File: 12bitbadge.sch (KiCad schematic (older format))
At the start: 44 parts, among them J1 Conn_02x04_Counter_Clockwise, J2 Conn_02x04_Counter_Clockwise, J3 Conn_02x04_Counter_Clockwise, J4 Conn_02x03_Odd_Even, J5 Conn_02x03_Odd_Even, J6 Conn_02x03_Odd_Even, J7 Conn_02x03_Odd_Even, SW1 SW_SPDT, SW10 SW_SPDT, SW11 SW_SPDT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

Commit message: Updated to hand-solderable SMD
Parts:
- R1, R10, R11, R12, R13, R14, R15, R16, R17, R18, R2, R3, R4, R5, R6, R7, R8, R9: footprint Resistor_SMD:R_0805_2012Metric -> Resistor_SMD:R_0805_2012Metric_Pad1.15x1.40mm_HandSolder
- U1, U2, U3: footprint Package_TO_SOT_SMD:SOT-23-6 -> Package_TO_SOT_SMD:SOT-23-6_Handsoldering
- U4, U5, U6: footprint Package_TO_SOT_SMD:SOT-23-5 -> Package_TO_SOT_SMD:SOT-23-5_HandSoldering
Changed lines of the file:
@@
 F 0 "U1" H 2700 1325 50  0000 R CNN
 F 1 "ATtiny10-TS" H 2700 1250 50  0000 R CNN
-F 2 "Package_TO_SOT_SMD:SOT-23-6" H 2725 1300 50  0001 C CIN
+F 2 "Package_TO_SOT_SMD:SOT-23-6_Handsoldering" H 2725 1300 50  0001 C CIN
 F 3 "http://ww1.microchip.com/downloads/en/DeviceDoc/Atmel-8127-AVR-8-bit-Microcontroller-ATtiny4-ATtiny5-ATtiny9-ATtiny10_Datasheet.pdf" H 2725 1300 50  0001 C CNN
 	1    2725 1300
@@
 F 0 "U2" H 2400 3100 50  0000 R CNN
 F 1 "ATtiny10-TS" H 2700 3000 50  0000 R CNN
-F 2 "Package_TO_SOT_SMD:SOT-23-6" H 2725 3050 50  0001 C CIN
+F 2 "Package_TO_SOT_SMD:SOT-23-6_Handsoldering" H 2725 3050 50  0001 C CIN
 F 3 "http://ww1.microchip.com/downloads/en/DeviceDoc/Atmel-8127-AVR-8-bit-Microcontroller-ATtiny4-ATtiny5-ATtiny9-ATtiny10_Datasheet.pdf" H 2725 3050 50  0001 C CNN
 	1    2725 3050
@@
 F 0 "U3" H 2375 5175 50  0000 R CNN
 F 1 "ATtiny10-TS" H 2550 5075 50  0000 R CNN
-F 2 "Package_TO_SOT_SMD:SOT-23-6" H 2575 5125 50  0001 C CIN
+F 2 "Package_TO_SOT_SMD:SOT-23-6_Handsoldering" H 2575 5125 50  0001 C CIN
 F 3 "http://ww1.microchip.com/downloads/en/DeviceDoc/Atmel-8127-AVR-8-bit-Microcontroller-ATtiny4-ATtiny5-ATtiny9-ATtiny10_Datasheet.pdf" H 2575 5125 50  0001 C CNN
 	1    2575 5125
@@
 F 0 "R2" V 5943 950 50  0000 C CNN
 F 1 "50k" V 6034 950 50  0000 C CNN
-F 2 "Resistor_SMD:R_0805_2012Metric" V 6080 950 50  0001 C CNN
+F 2 "Resistor_SMD:R_0805_2012Metric_Pad1.15x1.40mm_HandSolder" V 6080 950 50  0001 C CNN
 F 3 "~" H 6150 950 50  0001 C CNN
 	1    6150 950
@@
 F 0 "R3" V 6768 950 50  0000 C CNN
 F 1 "100k" V 6859 950 50  0000 C CNN
-F 2 "Resistor_SMD:R_0805_2012Metric" V 6905 950 50  0001 C CNN
+F 2 "Resistor_SMD:R_0805_2012Metric_Pad1.15x1.40mm_HandSolder" V 6905 950 50  0001 C CNN
 F 3 "~" H 6975 950 50  0001 C CNN
 	1    6975 950
@@
 F 0 "R4" V 7593 950 50  0000 C CNN
 F 1 "200k" V 7684 950 50  0000 C CNN
-F 2 "Resistor_SMD:R_0805_2012Metric" V 7730 950 50  0001 C CNN
+F 2 "Resistor_SMD:R_0805_2012Metric_Pad1.15x1.40mm_HandSolder" V 7730 950 50  0001 C CNN
 F 3 "~" H 7800 950 50  0001 C CNN
 	1    7800 950
@@
 F 0 "R1" V 5118 950 50  0000 C CNN
 F 1 "25k" V 5209 950 50  0000 C CNN
-F 2 "Resistor_SMD:R_0805_2012Metric" V 5255 950 50  0001 C CNN
+F 2 "Resistor_SMD:R_0805_2012Metric_Pad1.15x1.40mm_HandSolder" V 5255 950 50  0001 C CNN
 F 3 "~" H 5325 950 50  0001 C CNN
 	1    5325 950
@@
 F 0 "R5" H 8430 1254 50  0000 R CNN
 F 1 "25k" H 8430 1345 50  0000 R CNN
-F 2 "Resistor_SMD:R_0805_2012Metric" V 8430 1300 50  0001 C CNN
+F 2 "Resistor_SMD:R_0805_2012Metric_Pad1.15x1.40mm_HandSolder" V 8430 1300 50  0001 C CNN
 F 3 "~" H 8500 1300 50  0001 C CNN
 	1    8500 1300
@@
 F 0 "R7" V 5943 2850 50  0000 C CNN
 F 1 "50k" V 6034 2850 50  0000 C CNN
-F 2 "Resistor_SMD:R_0805_2012Metric" V 6080 2850 50  0001 C CNN
+F 2 "Resistor_SMD:R_0805_2012Metric_Pad1.15x1.40mm_HandSolder" V 6080 2850 50  0001 C CNN
 F 3 "~" H 6150 2850 50  0001 C CNN
 	1    6150 2850
@@
 F 0 "R8" V 6768 2850 50  0000 C CNN
 F 1 "100k" V 6859 2850 50  0000 C CNN
-F 2 "Resistor_SMD:R_0805_2012Metric" V 6905 2850 50  0001 C CNN
+F 2 "Resistor_SMD:R_0805_2012Metric_Pad1.15x1.40mm_HandSolder" V 6905 2850 50  0001 C CNN
 F 3 "~" H 6975 2850 50  0001 C CNN
 	1    6975 2850
@@
 F 0 "R9" V 7593 2850 50  0000 C CNN
 F 1 "200k" V 7684 2850 50  0000 C CNN
-F 2 "Resistor_SMD:R_0805_2012Metric" V 7730 2850 50  0001 C CNN
+F 2 "Resistor_SMD:R_0805_2012Metric_Pad1.15x1.40mm_HandSolder" V 7730 2850 50  0001 C CNN
 F 3 "~" H 7800 2850 50  0001 C CNN
 	1    7800 2850
@@
 F 0 "R6" V 5118 2850 50  0000 C CNN
 F 1 "25k" V 5209 2850 50  0000 C CNN
-F 2 "Resistor_SMD:R_0805_2012Metric" V 5255 2850 50  0001 C CNN
+F 2 "Resistor_SMD:R_0805_2012Metric_Pad1.15x1.40mm_HandSolder" V 5255 2850 50  0001 C CNN
 F 3 "~" H 5325 2850 50  0001 C CNN
 	1    5325 2850
@@
 F 0 "R10" H 8430 3154 50  0000 R CNN
 F 1 "25k" H 8430 3245 50  0000 R CNN
-F 2 "Resistor_SMD:R_0805_2012Metric" V 8430 3200 50  0001 C CNN
+F 2 "Resistor_SMD:R_0805_2012Metric_Pad1.15x1.40mm_HandSolder" V 8430 3200 50  0001 C CNN
 F 3 "~" H 8500 3200 50  0001 C CNN
 	1    8500 3200
@@
 F 0 "R12" V 5768 5025 50  0000 C CNN
 F 1 "50k" V 5859 5025 50  0000 C CNN
-F 2 "Resistor_SMD:R_0805_2012Metric" V 5905 5025 50  0001 C CNN
+F 2 "Resistor_SMD:R_0805_2012Metric_Pad1.15x1.40mm_HandSolder" V 5905 5025 50  0001 C CNN
 F 3 "~" H 5975 5025 50  0001 C CNN
 	1    5975 5025
@@
 F 0 "R13" V 6593 5025 50  0000 C CNN
 F 1 "100k" V 6684 5025 50  0000 C CNN
-F 2 "Resistor_SMD:R_0805_2012Metric" V 6730 5025 50  0001 C CNN
+F 2 "Resistor_SMD:R_0805_2012Metric_Pad1.15x1.40mm_HandSolder" V 6730 5025 50  0001 C CNN
 F 3 "~" H 6800 5025 50  0001 C CNN
 	1    6800 5025
@@
 F 0 "R14" V 7418 5025 50  0000 C CNN
 F 1 "200k" V 7509 5025 50  0000 C CNN
-F 2 "Resistor_SMD:R_0805_2012Metric" V 7555 5025 50  0001 C CNN
+F 2 "Resistor_SMD:R_0805_2012Metric_Pad1.15x1.40mm_HandSolder" V 7555 5025 50  0001 C CNN
 F 3 "~" H 7625 5025 50  0001 C CNN
 	1    7625 5025
@@
 F 0 "R11" V 4943 5025 50  0000 C CNN
 F 1 "25k" V 5034 5025 50  0000 C CNN
-F 2 "Resistor_SMD:R_0805_2012Metric" V 5080 5025 50  0001 C CNN
+F 2 "Resistor_SMD:R_0805_2012Metric_Pad1.15x1.40mm_HandSolder" V 5080 5025 50  0001 C CNN
 F 3 "~" H 5150 5025 50  0001 C CNN
 	1    5150 5025
@@
 F 0 "R15" H 8255 5329 50  0000 R CNN
 F 1 "25k" H 8255 5420 50  0000 R CNN
-F 2 "Resistor_SMD:R_0805_2012Metric" V 8255 5375 50  0001 C CNN
+F 2 "Resistor_SMD:R_0805_2012Metric_Pad1.15x1.40mm_HandSolder" V 8255 5375 50  0001 C CNN
 F 3 "~" H 8325 5375 50  0001 C CNN
 	1    8325 5375
@@
 F 0 "R16" V 3550 7125 50  0000 C CNN
 F 1 "1k" V 3625 7125 50  0000 C CNN
-F 2 "Resistor_SMD:R_0805_2012Metric" V 3555 7125 50  0001 C CNN
+F 2 "Resistor_SMD:R_0805_2012Metric_Pad1.15x1.40mm_HandSolder" V 3555 7125 50  0001 C CNN
 F 3 "~" H 3625 7125 50  0001 C CNN
 	1    3625 7125
@@
 F 0 "R17" V 3550 7325 50  0000 C CNN
 F 1 "1k" V 3625 7325 50  0000 C CNN
-F 2 "Resistor_SMD:R_0805_2012Metric" V 3555 7325 50  0001 C CNN
+F 2 "Resistor_SMD:R_0805_2012Metric_Pad1.15x1.40mm_HandSolder" V 3555 7325 50  0001 C CNN
 F 3 "~" H 3625 7325 50  0001 C CNN
 	1    3625 7325
@@
 F 0 "R18" V 3550 7525 50  0000 C CNN
 F 1 "1k" V 3625 7525 50  0000 C CNN
-F 2 "Resistor_SMD:R_0805_2012Metric" V 3555 7525 50  0001 C CNN
+F 2 "Resistor_SMD:R_0805_2012Metric_Pad1.15x1.40mm_HandSolder" V 3555 7525 50  0001 C CNN
 F 3 "~" H 3625 7525 50  0001 C CNN
 	1    3625 7525
@@
 F 0 "U4" H 10025 1817 50  0000 C CNN
 F 1 "TPS2041B" H 10025 1726 50  0000 C CNN
-F 2 "Package_TO_SOT_SMD:SOT-23-5" H 10025 1850 50  0001 C CNN
+F 2 "Package_TO_SOT_SMD:SOT-23-5_HandSoldering" H 10025 1850 50  0001 C CNN
 F 3 "http://www.ti.com/lit/ds/symlink/tps2041.pdf" H 9975 1650 50  0001 C CNN
 	1    10025 1350
@@
 F 0 "U5" H 10075 3792 50  0000 C CNN
 F 1 "TPS2041B" H 10075 3701 50  0000 C CNN
-F 2 "Package_TO_SOT_SMD:SOT-23-5" H 10075 3825 50  0001 C CNN
+F 2 "Package_TO_SOT_SMD:SOT-23-5_HandSoldering" H 10075 3825 50  0001 C CNN
 F 3 "http://www.ti.com/lit/ds/symlink/tps2041.pdf" H 10025 3625 50  0001 C CNN
 	1    10075 3325
@@
 F 0 "U6" H 10000 5992 50  0000 C CNN
 F 1 "TPS2041B" H 10000 5901 50  0000 C CNN
-F 2 "Package_TO_SOT_SMD:SOT-23-5" H 10000 6025 50  0001 C CNN
+F 2 "Package_TO_SOT_SMD:SOT-23-5_HandSoldering" H 10000 6025 50  0001 C CNN
 F 3 "http://www.ti.com/lit/ds/symlink/tps2041.pdf" H 9950 5825 50  0001 C CNN
 	1    10000 5525

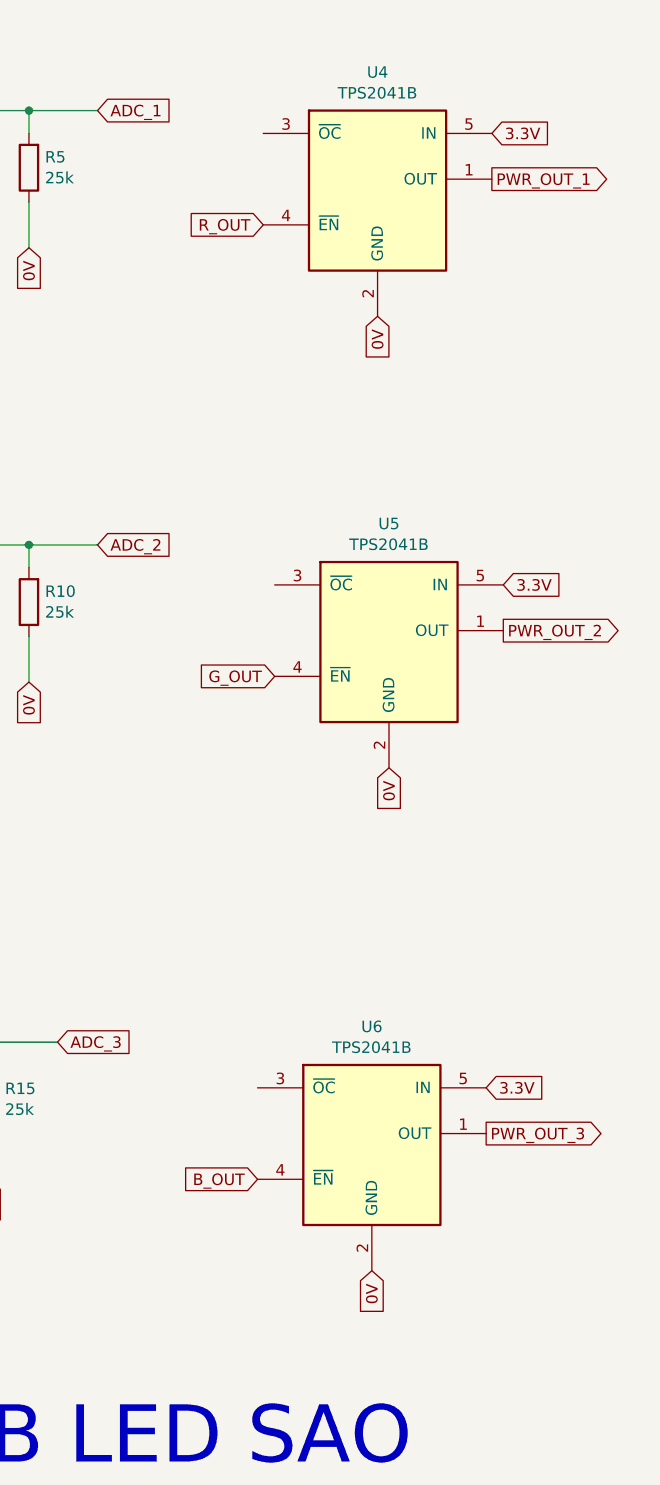
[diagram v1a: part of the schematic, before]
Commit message: Replaced switches with PWM-friendly MOSFETs
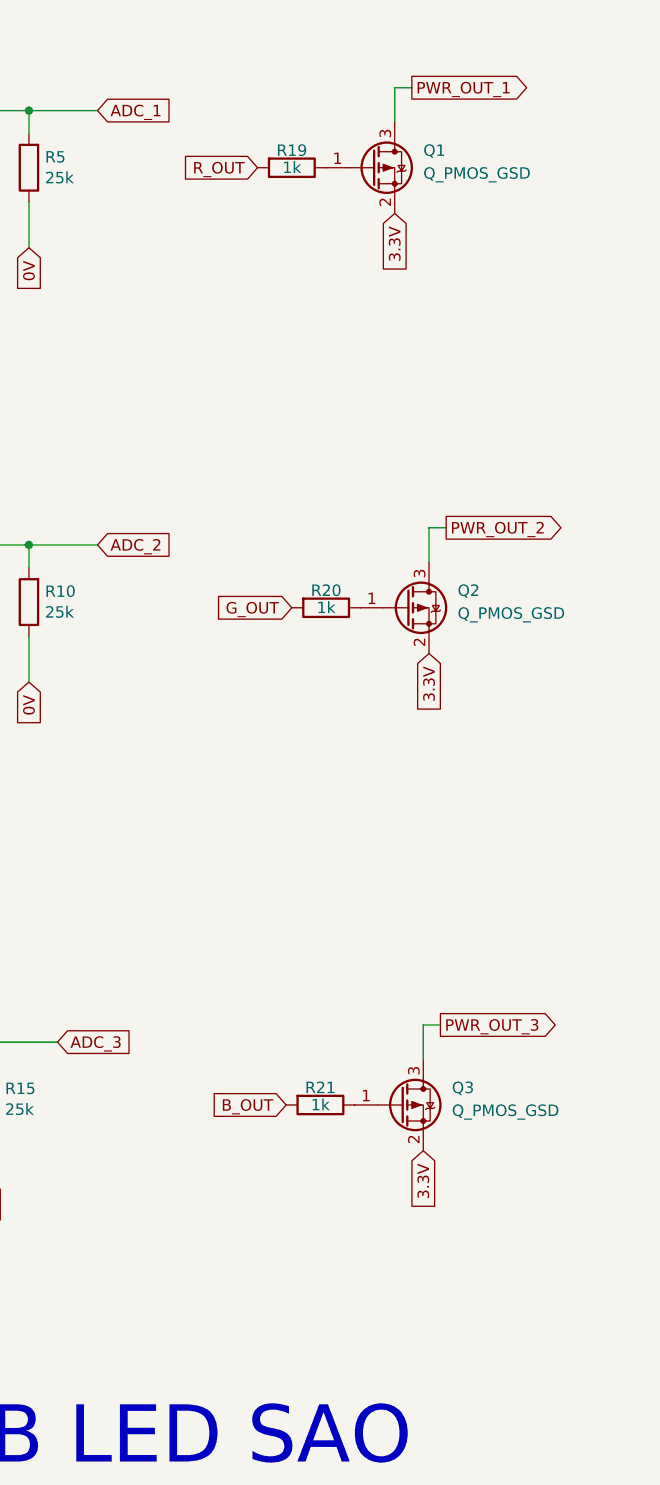
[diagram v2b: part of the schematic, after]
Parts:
- removed U4, U5, U6: TPS2041B, Package_TO_SOT_SMD:SOT-23-5_HandSoldering, symbol Power_Management:TPS2041B
- added Q1, Q2, Q3: Q_PMOS_GSD, Package_TO_SOT_SMD:SOT-23, symbol Device:Q_PMOS_GSD
- added R19, R20, R21: 1k, Resistor_SMD:R_0805_2012Metric_Pad1.15x1.40mm_HandSolder, symbol Device:R
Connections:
- net 3.3V: now also Q1.2 (S), Q2.2 (S), Q3.2 (S)
- net B_OUT: now also R21.2
- net G_OUT: now also R20.2
- net PWR_OUT_1: now also Q1.3 (D)
- net PWR_OUT_2: now also Q2.3 (D)
- net PWR_OUT_3: now also Q3.3 (D)
- net R_OUT: now also R19.2
- new net: Q2.1 (G), R20.1
- new net: Q1.1 (G), R19.1
- new net: Q3.1 (G), R21.1
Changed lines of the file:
@@
 Text GLabel 5950 5650 0    50   Input ~ 0
 PWR_OUT_3
-$Comp
-L Power_Management:TPS2041B U4
-U 1 1 5E3447C3
-P 10025 1350
-F 0 "U4" H 10025 1817 50  0000 C CNN
-F 1 "TPS2041B" H 10025 1726 50  0000 C CNN
-F 2 "Package_TO_SOT_SMD:SOT-23-5_HandSoldering" H 10025 1850 50  0001 C CNN
-F 3 "http://www.ti.com/lit/ds/symlink/tps2041.pdf" H 9975 1650 50  0001 C CNN
-	1    10025 1350
-	1    0    0    -1
-$EndComp
-Text GLabel 10025 1950 3    50   Input ~ 0
-0V
-Text GLabel 10525 1150 2    50   Input ~ 0
-3.3V
-Text GLabel 10525 1350 2    50   Output ~ 0
+Text GLabel 10175 950  2    50   Output ~ 0
 PWR_OUT_1
-Text GLabel 9525 1550 0    50   Input ~ 0
+Text GLabel 9500 1300 0    50   Input ~ 0
 R_OUT
-$Comp
-L Power_Management:TPS2041B U5
-U 1 1 5E3D9D27
-P 10075 3325
-F 0 "U5" H 10075 3792 50  0000 C CNN
-F 1 "TPS2041B" H 10075 3701 50  0000 C CNN
-F 2 "Package_TO_SOT_SMD:SOT-23-5_HandSoldering" H 10075 3825 50  0001 C CNN
-F 3 "http://www.ti.com/lit/ds/symlink/tps2041.pdf" H 10025 3625 50  0001 C CNN
-	1    10075 3325
-	1    0    0    -1
-$EndComp
-Text GLabel 10075 3925 3    50   Input ~ 0
-0V
-Text GLabel 10575 3125 2    50   Input ~ 0
-3.3V
-Text GLabel 10575 3325 2    50   Output ~ 0
+Text GLabel 10325 2875 2    50   Output ~ 0
 PWR_OUT_2
-Text GLabel 9575 3525 0    50   Input ~ 0
+Text GLabel 9650 3225 0    50   Input ~ 0
 G_OUT
-$Comp
-L Power_Management:TPS2041B U6
-U 1 1 5E3DDBE5
-P 10000 5525
-F 0 "U6" H 10000 5992 50  0000 C CNN
-F 1 "TPS2041B" H 10000 5901 50  0000 C CNN
-F 2 "Package_TO_SOT_SMD:SOT-23-5_HandSoldering" H 10000 6025 50  0001 C CNN
-F 3 "http://www.ti.com/lit/ds/symlink/tps2041.pdf" H 9950 5825 50  0001 C CNN
-	1    10000 5525
-	1    0    0    -1
-$EndComp
-Text GLabel 10000 6125 3    50   Input ~ 0
-0V
-Text GLabel 10500 5325 2    50   Input ~ 0
-3.3V
-Text GLabel 10500 5525 2    50   Output ~ 0
+Text GLabel 10300 5050 2    50   Output ~ 0
 PWR_OUT_3
-Text GLabel 9500 5725 0    50   Input ~ 0
+Text GLabel 9625 5400 0    50   Input ~ 0
 B_OUT
 Text GLabel 3950 7525 2    50   Input ~ 0
@@
 Text Label 1475 5150 0    50   ~ 0
 tpi_clk_3
+$Comp
+L Device:R R20
+U 1 1 5E2DF577
+P 9800 3225
+F 0 "R20" V 9725 3225 50  0000 C CNN
+F 1 "1k" V 9800 3225 50  0000 C CNN
+F 2 "Resistor_SMD:R_0805_2012Metric_Pad1.15x1.40mm_HandSolder" V 9730 3225 50  0001 C CNN
+F 3 "~" H 9800 3225 50  0001 C CNN
+	1    9800 3225
+	0    1    1    0
+$EndComp
+$Comp
+L Device:Q_PMOS_GSD Q2
+U 1 1 5E2E141C
+P 10150 3225
+F 0 "Q2" H 10375 3300 50  0000 L CNN
+F 1 "Q_PMOS_GSD" H 10375 3200 50  0000 L CNN
+F 2 "Package_TO_SOT_SMD:SOT-23" H 10350 3325 50  0001 C CNN
+F 3 "~" H 10150 3225 50  0001 C CNN
+	1    10150 3225
+	1    0    0    -1
+$EndComp
+Text GLabel 10250 3425 3    50   Input ~ 0
+3.3V
+Wire Wire Line
+	10325 2875 10250 2875
+Wire Wire Line
+	10250 2875 10250 3025
+$Comp
+L Device:R R19
+U 1 1 5E2F1A21
+P 9650 1300
+F 0 "R19" V 9575 1300 50  0000 C CNN
+F 1 "1k" V 9650 1300 50  0000 C CNN
+F 2 "Resistor_SMD:R_0805_2012Metric_Pad1.15x1.40mm_HandSolder" V 9580 1300 50  0001 C CNN
+F 3 "~" H 9650 1300 50  0001 C CNN
+	1    9650 1300
+	0    1    1    0
+$EndComp
+$Comp
+L Device:Q_PMOS_GSD Q1
+U 1 1 5E2F1A27
+P 10000 1300
+F 0 "Q1" H 10225 1375 50  0000 L CNN
+F 1 "Q_PMOS_GSD" H 10225 1275 50  0000 L CNN
+F 2 "Package_TO_SOT_SMD:SOT-23" H 10200 1400 50  0001 C CNN
+F 3 "~" H 10000 1300 50  0001 C CNN
+	1    10000 1300
+	1    0    0    -1
+$EndComp
+Text GLabel 10100 1500 3    50   Input ~ 0
+3.3V
+Wire Wire Line
+	10175 950  10100 950
+Wire Wire Line
+	10100 950  10100 1100
+$Comp
+L Device:R R21
+U 1 1 5E2F82CB
+P 9775 5400
+F 0 "R21" V 9700 5400 50  0000 C CNN
+F 1 "1k" V 9775 5400 50  0000 C CNN
+F 2 "Resistor_SMD:R_0805_2012Metric_Pad1.15x1.40mm_HandSolder" V 9705 5400 50  0001 C CNN
+F 3 "~" H 9775 5400 50  0001 C CNN
+	1    9775 5400
+	0    1    1    0
+$EndComp
+$Comp
+L Device:Q_PMOS_GSD Q3
+U 1 1 5E2F82D1
+P 10125 5400
+F 0 "Q3" H 10350 5475 50  0000 L CNN
+F 1 "Q_PMOS_GSD" H 10350 5375 50  0000 L CNN
+F 2 "Package_TO_SOT_SMD:SOT-23" H 10325 5500 50  0001 C CNN
+F 3 "~" H 10125 5400 50  0001 C CNN
+	1    10125 5400
+	1    0    0    -1
+$EndComp
+Text GLabel 10225 5600 3    50   Input ~ 0
+3.3V
+Wire Wire Line
+	10300 5050 10225 5050
+Wire Wire Line
+	10225 5050 10225 5200
 $EndSCHEMATC

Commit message: Updated MOSFETs to hand-solderable pads
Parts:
- Q1, Q2, Q3: footprint Package_TO_SOT_SMD:SOT-23 -> Package_TO_SOT_SMD:SOT-23_Handsoldering
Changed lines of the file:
@@
 F 0 "Q2" H 10375 3300 50  0000 L CNN
 F 1 "Q_PMOS_GSD" H 10375 3200 50  0000 L CNN
-F 2 "Package_TO_SOT_SMD:SOT-23" H 10350 3325 50  0001 C CNN
+F 2 "Package_TO_SOT_SMD:SOT-23_Handsoldering" H 10350 3325 50  0001 C CNN
 F 3 "~" H 10150 3225 50  0001 C CNN
 	1    10150 3225
@@
 F 0 "Q1" H 10225 1375 50  0000 L CNN
 F 1 "Q_PMOS_GSD" H 10225 1275 50  0000 L CNN
-F 2 "Package_TO_SOT_SMD:SOT-23" H 10200 1400 50  0001 C CNN
+F 2 "Package_TO_SOT_SMD:SOT-23_Handsoldering" H 10200 1400 50  0001 C CNN
 F 3 "~" H 10000 1300 50  0001 C CNN
 	1    10000 1300
@@
 F 0 "Q3" H 10350 5475 50  0000 L CNN
 F 1 "Q_PMOS_GSD" H 10350 5375 50  0000 L CNN
-F 2 "Package_TO_SOT_SMD:SOT-23" H 10325 5500 50  0001 C CNN
+F 2 "Package_TO_SOT_SMD:SOT-23_Handsoldering" H 10325 5500 50  0001 C CNN
 F 3 "~" H 10125 5400 50  0001 C CNN
 	1    10125 5400
